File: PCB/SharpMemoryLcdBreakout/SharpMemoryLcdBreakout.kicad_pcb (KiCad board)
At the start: 2 copper layers, 14 x 40 mm, 10 parts, among them J1 EMD, J2 DISP, J3 EIN, J4 Conn_2Rows-05Pins, J5 FH12-10S-0.5SH

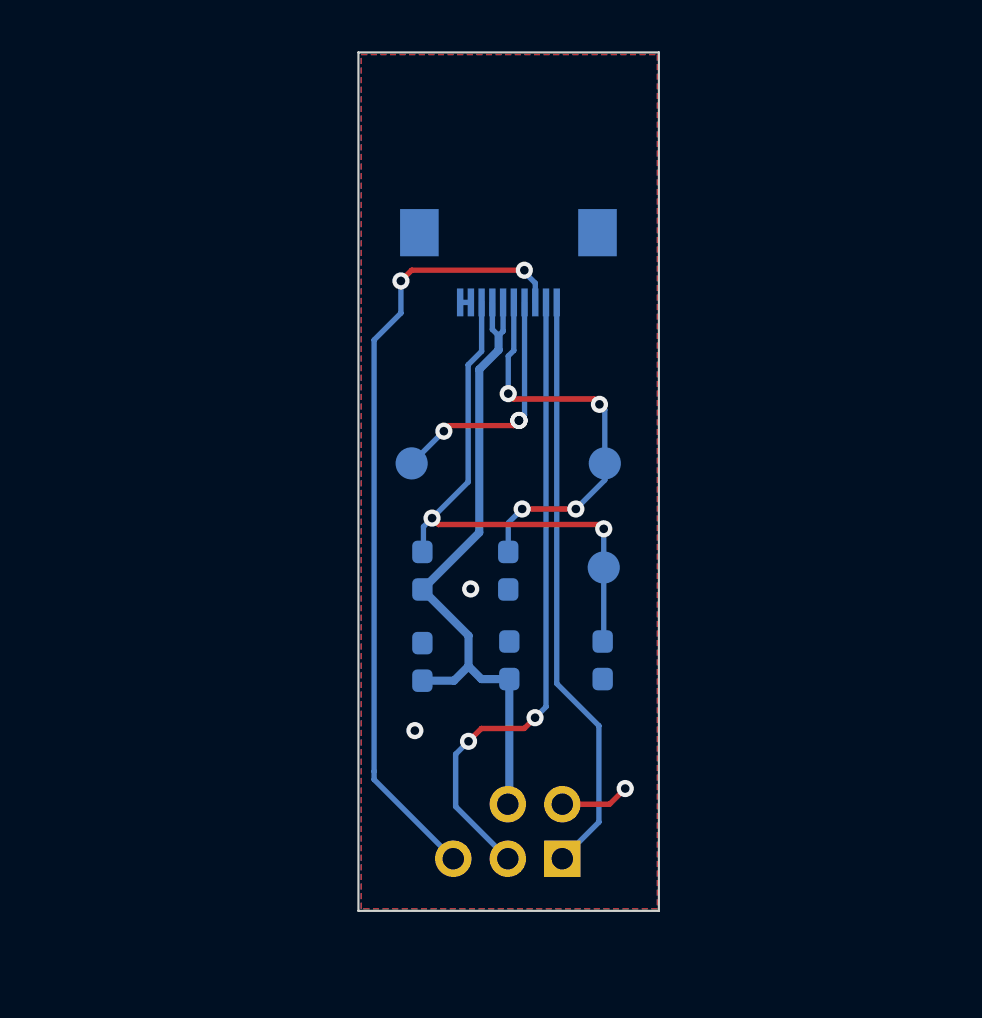
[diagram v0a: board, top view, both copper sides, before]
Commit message: increased size of pcb for smt assembly
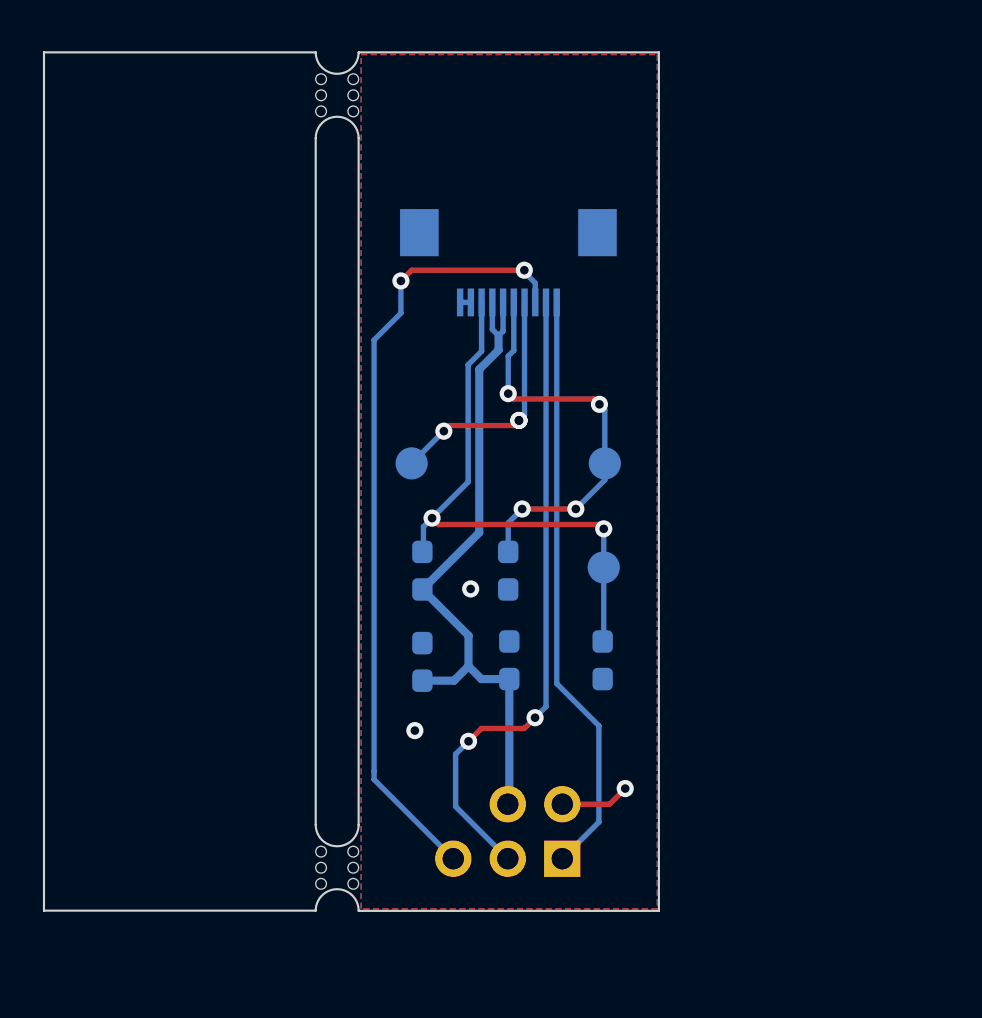
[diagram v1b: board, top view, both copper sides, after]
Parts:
- added mouse-bite-2mm-slot: VAL**, SharpMemoryLcdBreakout:mouse-bite-2mm-slot, F.Cu at (89.2, 74.1)
- added mouse-bite-2mm-slot: VAL**, SharpMemoryLcdBreakout:mouse-bite-2mm-slot, F.Cu at (89.2, 38.1)
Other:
- board size 14 x 40 mm -> 28.7 x 40 mm
- board text added: "Sharp Memory LCD Breakout v0.1"
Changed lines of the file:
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@@
       (outputformat 1)
       (mirror false)
-      (drillshape 1)
+      (drillshape 0)
       (scaleselection 1)
-      (outputdirectory "")
+      (outputdirectory "gerber/")
     )
   )
@@
   (net 7 "Net-(J4-Pad3)")
   (net 8 "Net-(J4-Pad1)")
+  (footprint "SharpMemoryLcdBreakout:mouse-bite-2mm-slot" (layer "F.Cu")
+    (at 89.23 74.14 90)
+    (attr through_hole)
+    (fp_text reference "mouse-bite-2mm-slot" (at 0 -2 90) (layer "F.SilkS") hide
+      (effects (font (size 1 1) (thickness 0.2)))
+    )
+    (fp_text value "VAL**" (at 0 2.1 90) (layer "F.SilkS") hide
+      (effects (font (size 1 1) (thickness 0.2)))
+    )
+    (fp_circle (center -2 0) (end -2 -0.06) (layer "Dwgs.User") (width 0.05) (fill none))
+    (fp_circle (center 2 0) (end 2.06 0) (layer "Dwgs.User") (width 0.05) (fill none))
+    (fp_line (start -2 0) (end -2 0) (layer "Eco1.User") (width 2))
+    (fp_line (start 2 0) (end 2 0) (layer "Eco1.User") (width 2))
+    (pad "" np_thru_hole circle (at 0 -0.75 90) (locked) (size 0.5 0.5) (drill 0.5) (layers *.Cu *.Mask))
+    (pad "" np_thru_hole circle (at -0.75 -0.75 90) (locked) (size 0.5 0.5) (drill 0.5) (layers *.Cu *.Mask))
+    (pad "" np_thru_hole circle (at -0.75 0.75 90) (locked) (size 0.5 0.5) (drill 0.5) (layers *.Cu *.Mask))
+    (pad "" np_thru_hole circle (at 0 0.75 90) (locked) (size 0.5 0.5) (drill 0.5) (layers *.Cu *.Mask))
+    (pad "" np_thru_hole circle (at 0.75 -0.75 90) (locked) (size 0.5 0.5) (drill 0.5) (layers *.Cu *.Mask))
+    (pad "" np_thru_hole circle (at 0.75 0.75 90) (locked) (size 0.5 0.5) (drill 0.5) (layers *.Cu *.Mask))
+  )
+  (footprint "SharpMemoryLcdBreakout:mouse-bite-2mm-slot" (layer "F.Cu")
+    (at 89.23 38.15 90)
+    (attr through_hole)
+    (fp_text reference "mouse-bite-2mm-slot" (at 0 -2 90) (layer "F.SilkS") hide
+      (effects (font (size 1 1) (thickness 0.2)))
+    )
+    (fp_text value "VAL**" (at 0 2.1 90) (layer "F.SilkS") hide
+      (effects (font (size 1 1) (thickness 0.2)))
+    )
+    (fp_circle (center -2 0) (end -2 -0.06) (layer "Dwgs.User") (width 0.05) (fill none))
+    (fp_circle (center 2 0) (end 2.06 0) (layer "Dwgs.User") (width 0.05) (fill none))
+    (fp_line (start -2 0) (end -2 0) (layer "Eco1.User") (width 2))
+    (fp_line (start 2 0) (end 2 0) (layer "Eco1.User") (width 2))
+    (pad "" np_thru_hole circle (at 0 -0.75 90) (locked) (size 0.5 0.5) (drill 0.5) (layers *.Cu *.Mask))
+    (pad "" np_thru_hole circle (at -0.75 -0.75 90) (locked) (size 0.5 0.5) (drill 0.5) (layers *.Cu *.Mask))
+    (pad "" np_thru_hole circle (at -0.75 0.75 90) (locked) (size 0.5 0.5) (drill 0.5) (layers *.Cu *.Mask))
+    (pad "" np_thru_hole circle (at 0 0.75 90) (locked) (size 0.5 0.5) (drill 0.5) (layers *.Cu *.Mask))
+    (pad "" np_thru_hole circle (at 0.75 -0.75 90) (locked) (size 0.5 0.5) (drill 0.5) (layers *.Cu *.Mask))
+    (pad "" np_thru_hole circle (at 0.75 0.75 90) (locked) (size 0.5 0.5) (drill 0.5) (layers *.Cu *.Mask))
+  )
   (footprint "TestPoint:TestPoint_Pad_D1.5mm" (layer "B.Cu")
     (at 92.7 55.3 180)
@@
       (net 6 "Net-(J4-Pad5)") (pinfunction "Pin_5"))
   )
-  (gr_rect (start 90.22 36.15) (end 104.22 76.15) (layer "Edge.Cuts") (width 0.1) (fill none))
+  (gr_line (start 90.230049 36.15) (end 104.22 36.15) (layer "Edge.Cuts") (width 0.1))
+  (gr_line (start 104.22 36.15) (end 104.22 76.15) (layer "Edge.Cuts") (width 0.1))
+  (gr_line (start 88.23 40.15) (end 88.229951 72.14) (layer "Edge.Cuts") (width 0.1))
+  (gr_line (start 90.230049 72.14) (end 90.23 40.15) (layer "Edge.Cuts") (width 0.1))
+  (gr_arc (start 89.23 72.14) (end 90.230049 72.14) (angle 180) (layer "Edge.Cuts") (width 0.1))
+  (gr_line (start 75.57 76.14) (end 75.57 36.15) (layer "Edge.Cuts") (width 0.1))
+  (gr_arc (start 89.230025 76.14) (end 90.23 76.15) (angle -180.572953) (layer "Edge.Cuts") (width 0.1))
+  (gr_arc (start 89.23 36.15) (end 90.230049 36.15) (angle 180) (layer "Edge.Cuts") (width 0.1))
+  (gr_line (start 88.229951 36.15) (end 75.57 36.15) (layer "Edge.Cuts") (width 0.1))
+  (gr_arc (start 89.23 40.15) (end 90.23 40.15) (angle -180) (layer "Edge.Cuts") (width 0.1))
+  (gr_line (start 90.23 76.15) (end 104.22 76.15) (layer "Edge.Cuts") (width 0.1))
+  (gr_line (start 88.23 76.14) (end 75.57 76.14) (layer "Edge.Cuts") (width 0.1))
   (gr_rect (start 90.22 37.05) (end 104.22 69.05) (layer "User.1") (width 0.01) (fill none))
   (gr_text "CS" (at 94.65 75.55) (layer "B.SilkS")
@@
     (effects (font (size 0.6 0.6) (thickness 0.1)) (justify mirror))
   )
+  (gr_text "Sharp Memory LCD \nBreakout v0.1" (at 97.2 50.4) (layer "B.SilkS")
+    (effects (font (size 0.6 0.6) (thickness 0.1)) (justify mirror))
+  )

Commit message: added pins for disp and emd
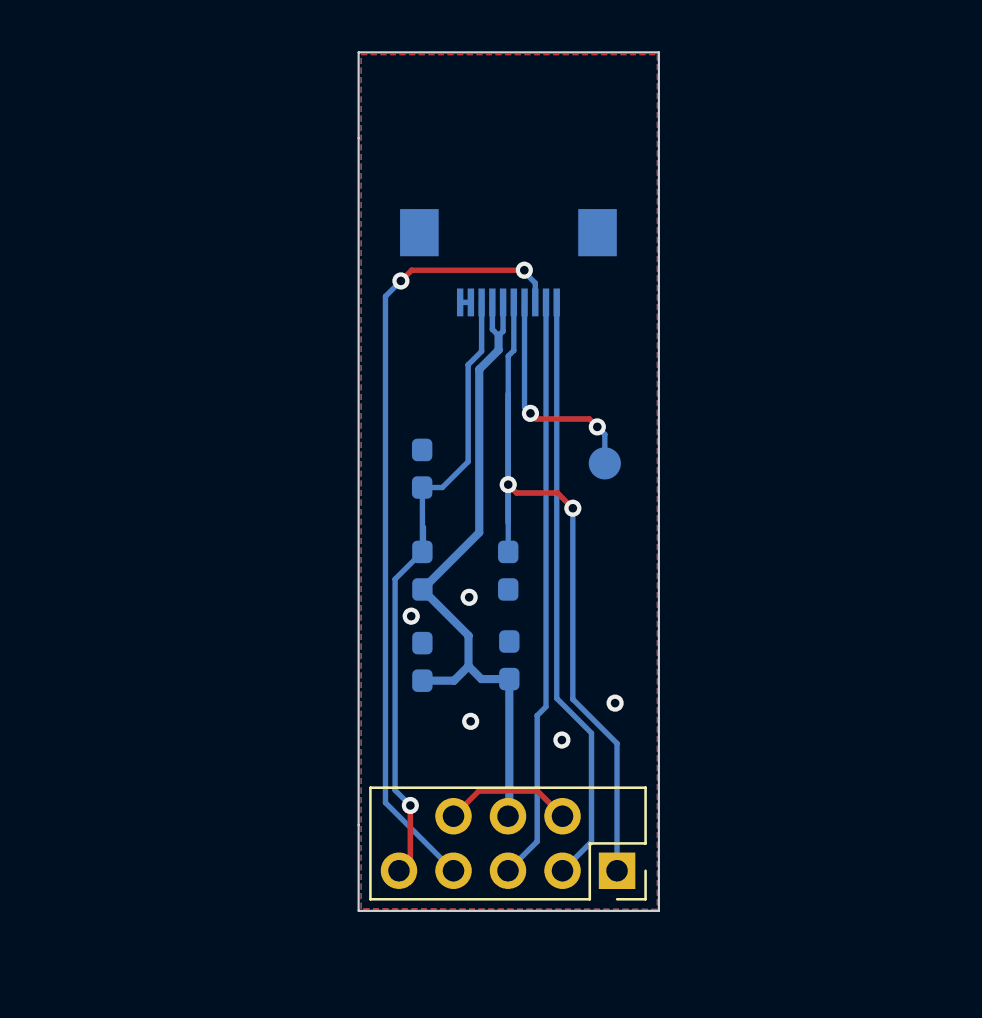
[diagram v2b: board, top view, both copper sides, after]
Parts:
- removed J3: EIN, TestPoint:TestPoint_Pad_D1.5mm
- removed J4: Conn_2Rows-05Pins, SharpMemoryLcdBreakout:PinHeader_2Rows-05Pins_P2.54mm_Vertical
- removed mouse-bite-2mm-slot (x2): VAL**, SharpMemoryLcdBreakout:mouse-bite-2mm-slot
- J1: value EMD -> Pin Header; footprint TestPoint:TestPoint_Pad_D1.5mm -> SharpMemoryLcdBreakout:PinSocket_2Row_5+3_P2.54mm_Vertical; moved to F.Cu
- moved J1 14.1 mm to (102.3, 74.3), turned to -90 degrees
- moved R1 12.3 mm to (93.2, 55.5), turned to 90 degrees
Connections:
- J1 pad 1: Net-(J1-Pad1) -> Net-(C1-Pad1)
- J2 pad 1: Net-(C1-Pad1) -> Net-(J5-Pad7)
- J5 pad 10: Net-(J4-Pad1) -> Net-(J5-Pad10)
- J5 pad 3: Net-(J1-Pad1) -> Net-(J5-Pad3)
- J5 pad 7: Net-(J3-Pad1) -> Net-(J5-Pad7)
- J5 pad 8: Net-(J4-Pad5) -> Net-(J5-Pad8)
- J5 pad 9: Net-(J4-Pad3) -> Net-(J5-Pad9)
- R1 pad 1: Net-(J1-Pad1) -> Net-(J5-Pad3)
- R2 pad 2: Net-(J1-Pad1) -> Net-(J5-Pad3)
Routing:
- net Net-(J5-Pad8): track 0.00 -> 36.8 mm, vias 0 -> 2
- net Net-(J4-Pad5): track 36.6 -> 0.00 mm, vias 2 -> 0
- net Net-(J5-Pad3): track 0.00 -> 30.4 mm, vias 0 -> 1
- net Net-(J4-Pad3): track 29.8 -> 0.00 mm, vias 2 -> 0
- net Net-(J5-Pad10): track 0.00 -> 27.7 mm
- net Net-(J4-Pad1): track 27.4 -> 0.00 mm
- net Net-(J5-Pad9): track 0.00 -> 27.2 mm
- net Net-(J1-Pad1): track 26.2 -> 0.00 mm, vias 2 -> 0
- net Net-(C1-Pad1): track 19.1 -> 39.0 mm, vias 4 -> 2
- net Net-(J3-Pad1): track 11.4 -> 0.00 mm, vias 3 -> 0
- net Net-(J5-Pad7): track 0.00 -> 10.5 mm, vias 0 -> 2
- net GND: track 3.73 -> 6.55 mm, vias 3 -> 5
- net +3V3: track 31.6 -> 32.1 mm
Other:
- board size 28.7 x 40 mm -> 14 x 40 mm
- board text added: "DISP"
- board text added: "EMD"
- board text added: "Sharp Memory LCD Breakout v0.2"
- board text removed: "Sharp Memory LCD Breakout v0.1"

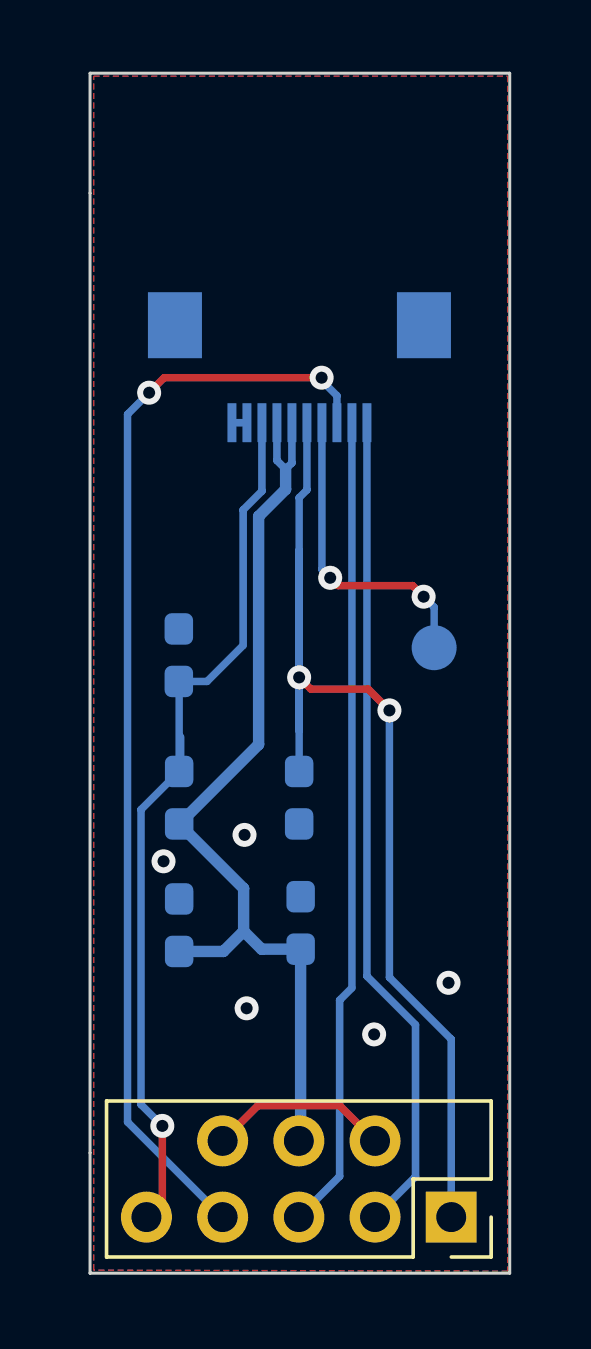
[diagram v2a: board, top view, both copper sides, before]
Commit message: switched EIN and EMD pin connections
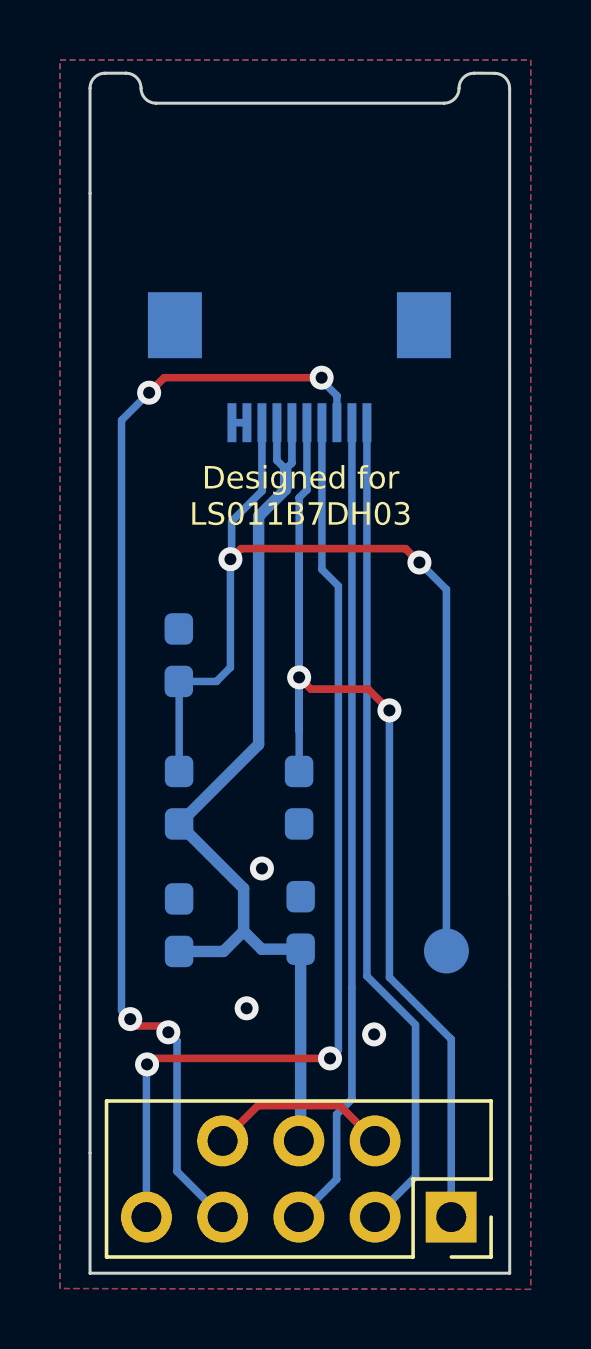
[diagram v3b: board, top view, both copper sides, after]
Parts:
- J2: value DISP -> EMD
- moved J2 10.1 mm to (102.1, 65.4)
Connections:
- J1 pad 5: Net-(J5-Pad3) -> Net-(J5-Pad7)
- J2 pad 1: Net-(J5-Pad7) -> Net-(J2-Pad1)
- J5 pad 3: Net-(J5-Pad3) -> Net-(J2-Pad1)
- R1 pad 1: Net-(J5-Pad3) -> Net-(J2-Pad1)
- R2 pad 2: Net-(J5-Pad3) -> Net-(J2-Pad1)
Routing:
- net Net-(J2-Pad1): track 0.00 -> 33.5 mm, vias 0 -> 2
- net Net-(J5-Pad3): track 30.4 -> 0.00 mm, vias 1 -> 0
- net Net-(J5-Pad7): track 10.5 -> 32.8 mm
- net Net-(J1-Pad4): track 36.8 -> 37.4 mm, vias 2 -> 4
- net GND: vias 5 -> 3
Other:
- outline, holes or cut-outs redrawn
- board text added: "Designed for LS011B7DH03"
- board text added: "EIN"
- board text added: "EXTMODE"
- board text added: "High"
- board text added: "Low"
- board text removed: "EMD"

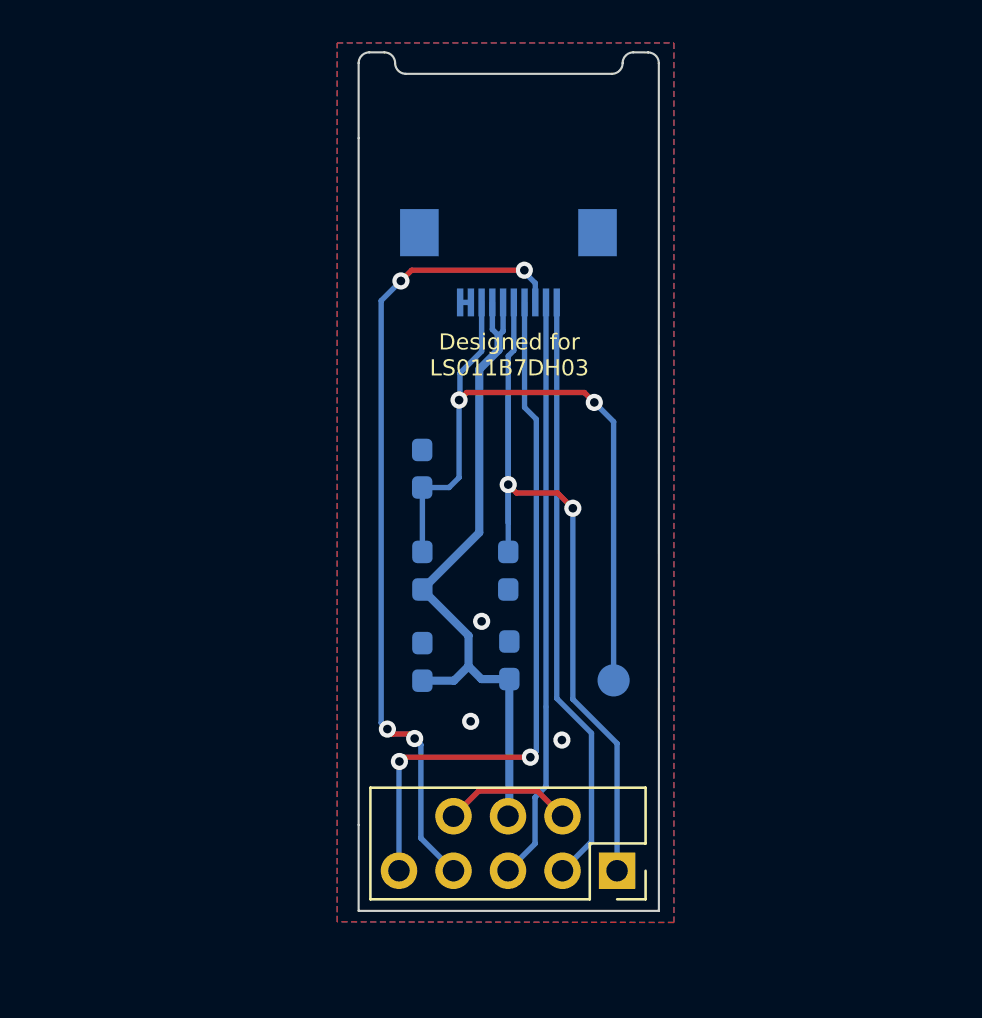
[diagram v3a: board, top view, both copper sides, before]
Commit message: Mirrored FPC pins
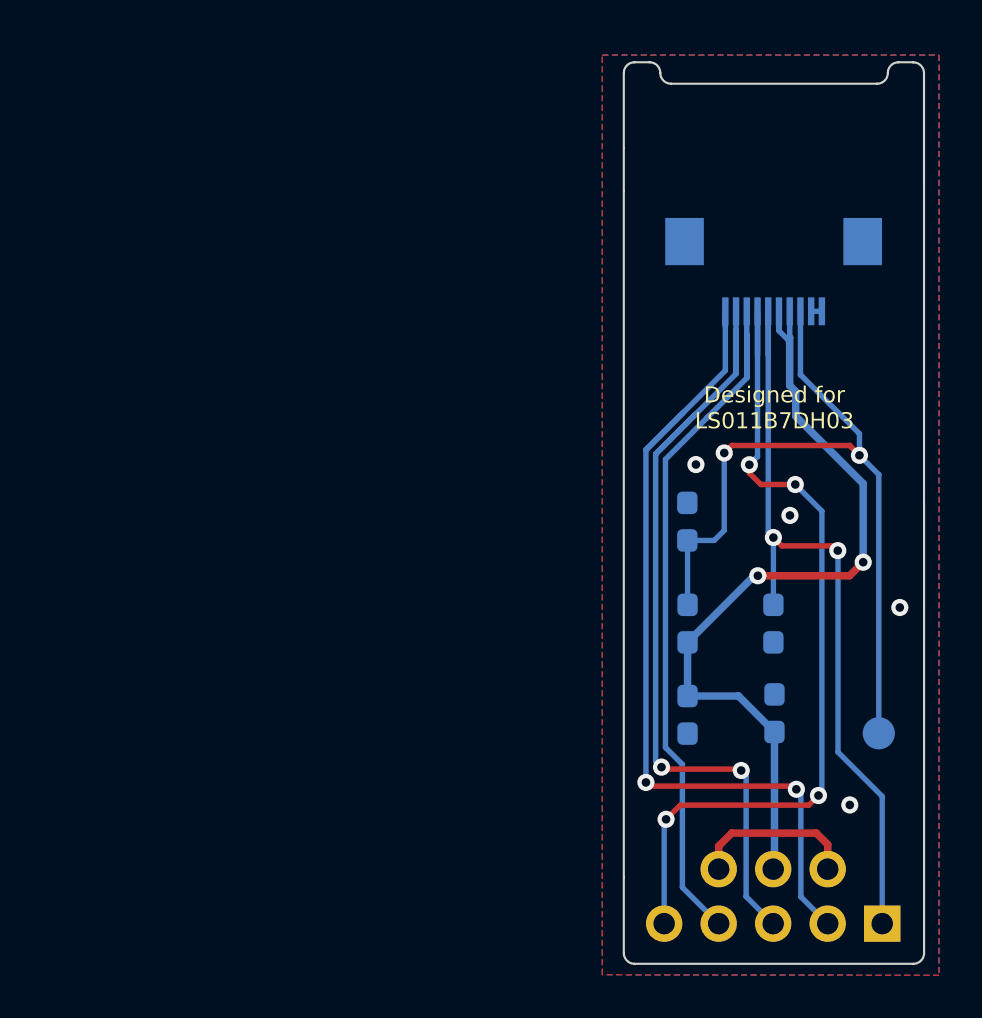
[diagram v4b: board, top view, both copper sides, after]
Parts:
- moved C1 12.6 mm to (109.6, 62.8)
- moved C2 12.6 mm to (109.6, 66.9)
- moved C3 12.6 mm to (105.6, 67.0), turned to -90 degrees
- moved J1 12.6 mm to (114.6, 76.7)
- moved J2 12.6 mm to (114.5, 67.9)
- moved R1 12.6 mm to (105.5, 58.0)
- moved R2 12.6 mm to (105.6, 62.8)
- moved J5 12.4 mm to (109.6, 46.4)
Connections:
- J1 pad 5: Net-(J5-Pad7) -> Net-(J1-Pad5)
- J5 pad 1: GND -> Net-(J1-Pad2)
- J5 pad 10: Net-(J1-Pad2) -> GND
- J5 pad 2: GND -> Net-(J1-Pad3)
- J5 pad 3: Net-(J2-Pad1) -> Net-(J1-Pad4)
- J5 pad 4: +3V3 -> Net-(J1-Pad5)
- J5 pad 5: +3V3 -> Net-(C1-Pad1)
- J5 pad 6: Net-(C1-Pad1) -> +3V3
- J5 pad 7: Net-(J5-Pad7) -> +3V3
- J5 pad 8: Net-(J1-Pad4) -> Net-(J2-Pad1)
- J5 pad 9: Net-(J1-Pad3) -> GND
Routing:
- net Net-(J1-Pad5): track 0.00 -> 39.6 mm, vias 0 -> 4
- net Net-(J5-Pad7): track 32.8 -> 0.00 mm, vias 2 -> 0
- net Net-(J1-Pad2): track 27.7 -> 40.7 mm, vias 0 -> 2
- net Net-(J1-Pad3): track 27.2 -> 39.1 mm, vias 0 -> 2
- net +3V3: track 32.1 -> 38.8 mm, vias 0 -> 2
- net Net-(J1-Pad4): track 37.4 -> 33.3 mm, vias 4 -> 0
- net Net-(J2-Pad1): track 33.5 -> 36.5 mm
- net GND: track 6.55 -> 8.27 mm, vias 3 -> 4
- net Net-(C1-Pad1): track 39.0 -> 37.3 mm
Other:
- board size 14 x 40 mm -> 14 x 42 mm
